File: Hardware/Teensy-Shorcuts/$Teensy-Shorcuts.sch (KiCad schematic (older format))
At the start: 21 parts, among them P1 CONN_01X01, P2 CONN_01X01, P3 CONN_01X01, P4 CONN_01X01, SW1 SW_PUSH, SW2 SW_PUSH, SW3 SW_PUSH, SW4 SW_PUSH, SW5 SW_PUSH, SW6 SW_PUSH, SW7 SW_PUSH, U1 Teensy_3.1

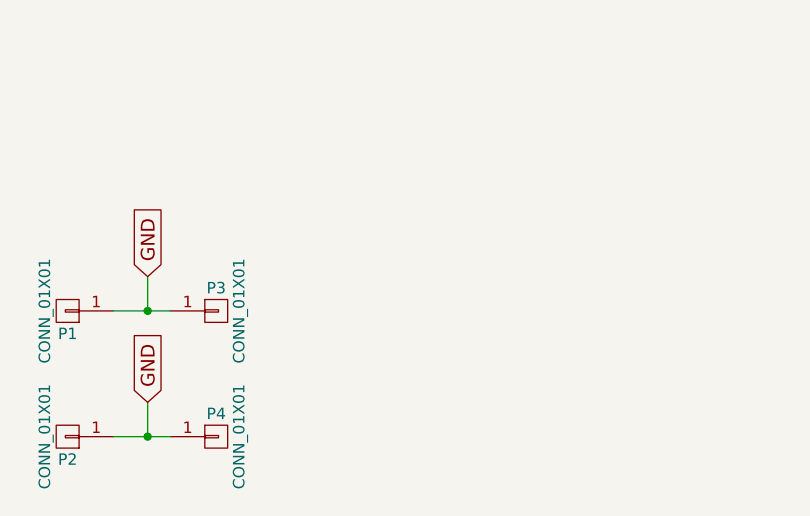
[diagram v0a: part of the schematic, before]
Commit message: Created Schematichs and PCB board layaot
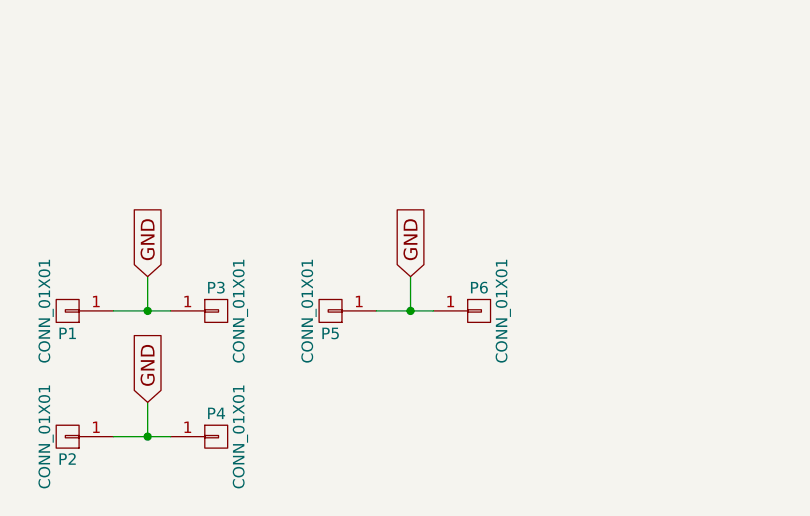
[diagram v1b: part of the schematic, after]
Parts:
- added P5, P6: CONN_01X01, Libraries:Jumper1x01, symbol CONN_01X01
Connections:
- net GND: now also P5.1 (P1), P6.1 (P1)
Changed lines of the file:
@@
 Wire Wire Line
 	9450 3200 9250 3200
+$Comp
+L CONN_01X01 P6
+U 1 1 5507311C
+P 3450 6300
+F 0 "P6" H 3450 6400 50  0000 C CNN
+F 1 "CONN_01X01" V 3550 6300 50  0000 C CNN
+F 2 "Libraries:Jumper1x01" H 3450 6300 60  0001 C CNN
+F 3 "" H 3450 6300 60  0000 C CNN
+	1    3450 6300
+	1    0    0    -1
+$EndComp
+$Comp
+L CONN_01X01 P5
+U 1 1 55073122
+P 2800 6300
+F 0 "P5" H 2800 6400 50  0000 C CNN
+F 1 "CONN_01X01" V 2900 6300 50  0000 C CNN
+F 2 "Libraries:Jumper1x01" H 2800 6300 60  0001 C CNN
+F 3 "" H 2800 6300 60  0000 C CNN
+	1    2800 6300
+	-1   0    0    1
+$EndComp
+Wire Wire Line
+	3000 6300 3250 6300
+Text GLabel 3150 6150 1    60   Input ~ 0
+GND
+Wire Wire Line
+	3150 6300 3150 6150
+Connection ~ 3150 6300
 $EndSCHEMATC
